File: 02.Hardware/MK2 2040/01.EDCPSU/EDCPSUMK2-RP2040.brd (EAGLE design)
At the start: 96 x 60.8 mm, 185 parts, among them J1 DX07S016JA1R1500, J6 Display, K1 FLEX CONNECTORES, Q2 2N7002PW, Q4 2N7002PW, Q5 2N7002PW, Q9 2N7002PW, U1 RP2040TR7, U10 IP2721, U11 AP63203, U12 AP64501SP-13, U2 MCP4725, U3 SN74AC14PWR, U4 MAX9938FEUK+T, U5 W25Q64JVSSIQ, U6 SN74AC14PWR, U7 TPIC2810D, U8 LM4040C25FTA, U9 MAX9064EUK+T, X1 ABM3C-12.000MHZ-D4Y-T

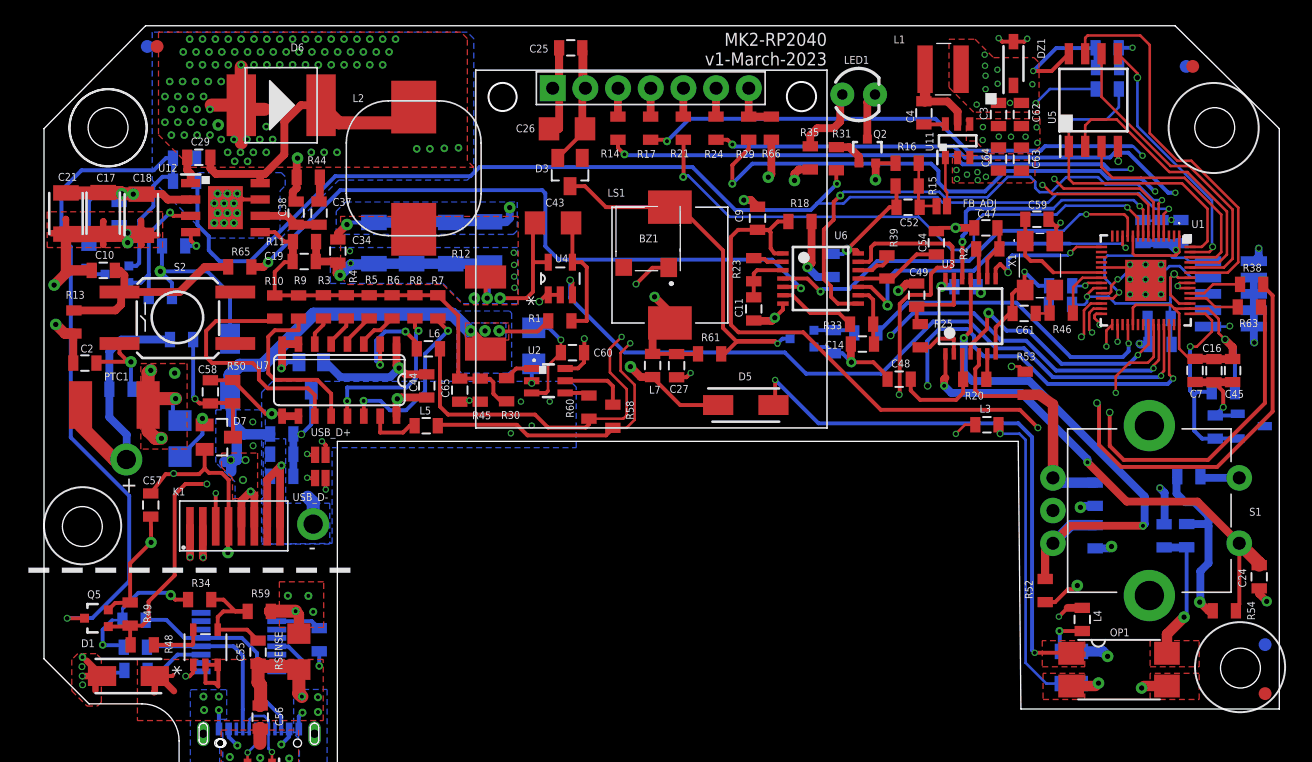
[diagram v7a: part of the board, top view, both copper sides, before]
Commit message: Añadido Test Pads
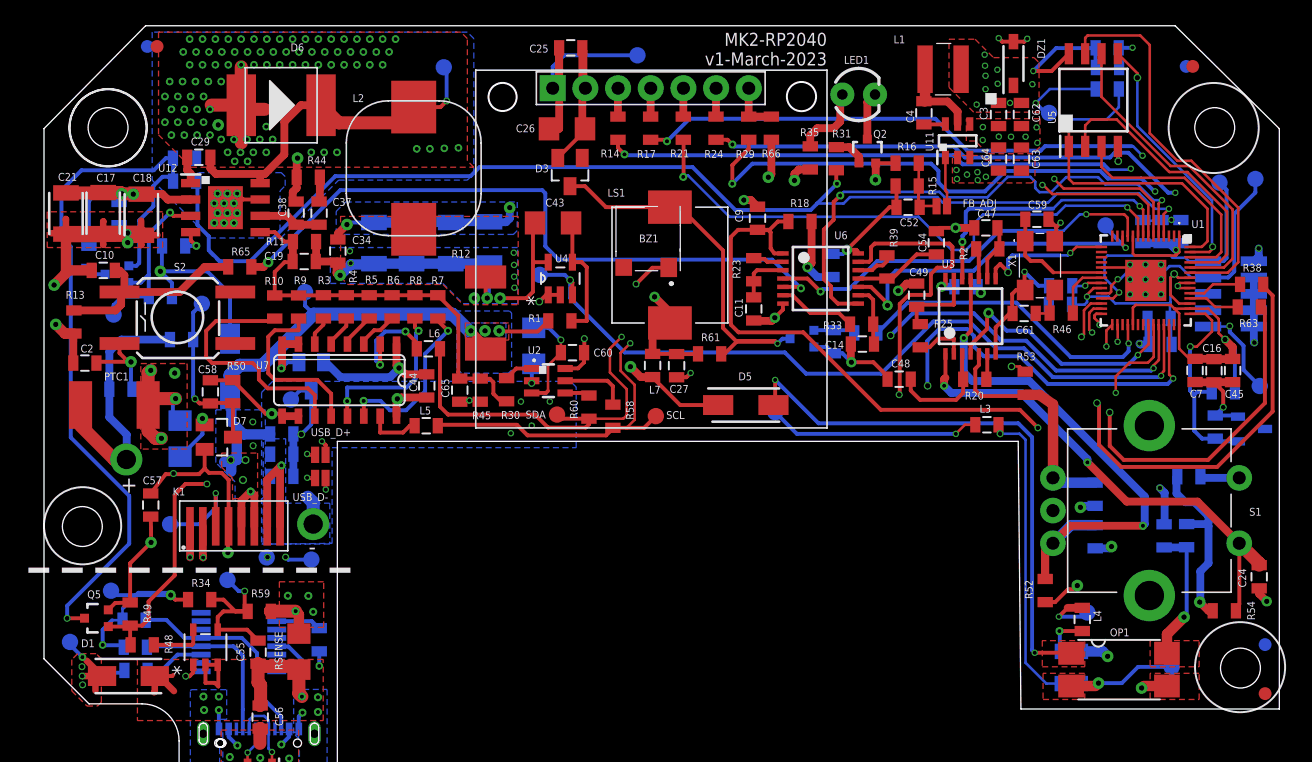
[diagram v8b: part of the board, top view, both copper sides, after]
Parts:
- added 3V3MCU, EN_TPS54531, GND, GND_IN, IN+, ISENSE, N$41, N$51, N$59, OVC_ALARM, PEDAL+, PEDAL-, RUN, SCL, SDA, SEL, SWCLK, SWDIO, USB-D+, USB-D-, VBUS_SENSE, VOSEN, VOUT: TESTPAD_TPSQB1,27, BeagleBone_Blue_R3:TESTPAD_B1,27
- R35: value 330R -> 130R
- R36: value 75K -> 27K
- R51: value 220K -> 390K
- moved U8 0.22 mm to (108.6, 41.5)
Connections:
- net 3V3MCU: now also 3V3MCU.TP
- net EN_TPS54531: now also EN_TPS54531.TP
- net GND: now also GND.TP
- net GND_IN: now also GND_IN.TP
- net IN+: now also IN+.TP
- net ISENSE: now also ISENSE.TP
- net N$41: now also N$41.TP
- net N$51: now also N$51.TP
- net N$59: now also N$59.TP
- net OVC_ALARM: now also OVC_ALARM.TP
- net PEDAL+: now also PEDAL+.TP
- net PEDAL-: now also PEDAL-.TP
- net RUN: now also RUN.TP
- net SCL: now also SCL.TP
- net SDA: now also SDA.TP
- net SEL: now also SEL.TP
- net SWCLK: now also SWCLK.TP
- net SWDIO: now also SWDIO.TP
- net USB_D+: now also USB-D+.TP
- net USB_D-: now also USB-D-.TP
- net VBUS_SENSE: now also VBUS_SENSE.TP
- net VOSEN: now also VOSEN.TP
- net VOUT: now also VOUT.TP
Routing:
- net PEDAL+: track 69.2 -> 83.9 mm
- net SWCLK: track 9.79 -> 19.9 mm
- net GND: track 220.8 -> 229.5 mm
- net SWDIO: track 13.0 -> 20.6 mm
- net N$41: track 3.44 -> 9.64 mm
- net RUN: track 19.0 -> 24.6 mm
- net N$51: track 23.1 -> 28.6 mm, vias 0 -> 1
- net SEL: track 84.8 -> 90.1 mm
- net GND_IN: track 47.9 -> 52.7 mm
- net EN_TPS54531: track 10.7 -> 14.5 mm
- net N$59: track 10.2 -> 13.6 mm, vias 0 -> 1
- net VBUS_SENSE: track 93.5 -> 96.6 mm
- net SCL: track 82.1 -> 84.7 mm
- net SDA: track 86.4 -> 89.1 mm
- net ISENSE: track 58.5 -> 61.1 mm
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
